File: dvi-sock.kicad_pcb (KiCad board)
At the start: 2 copper layers, 25.2 x 22.5 mm, 15 parts, among them J1 Conn_01x05, J2 Conn_01x05, J3 Conn_01x03, J4 NOT_HDMI_A, J5 2.54mm_2p_nofit

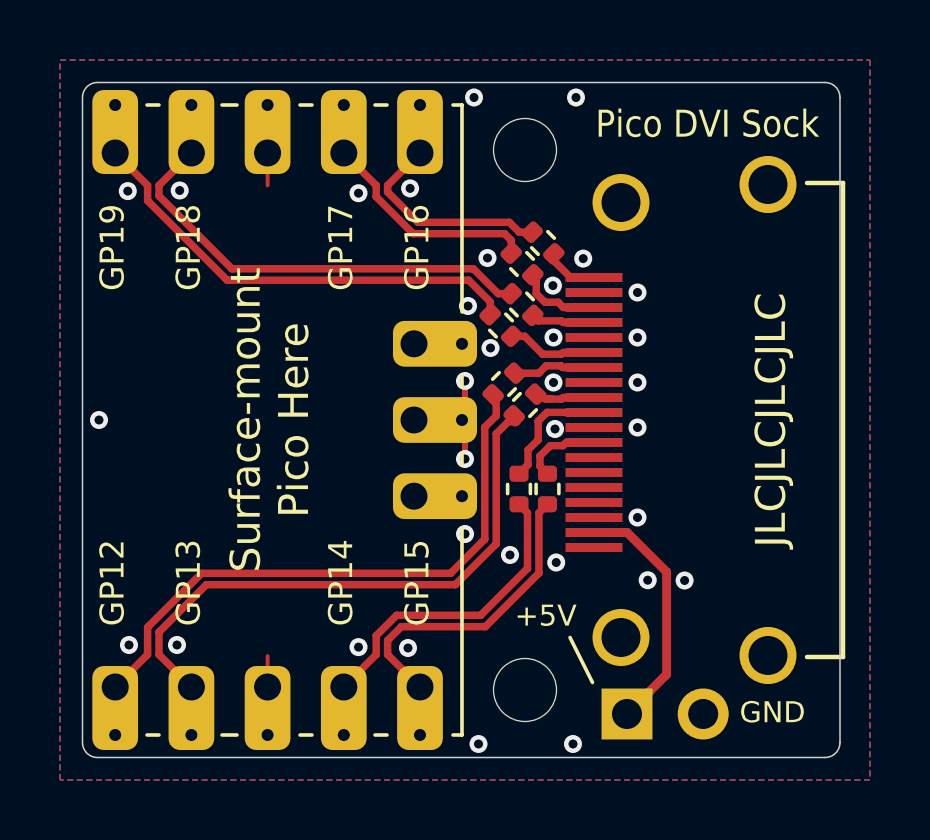
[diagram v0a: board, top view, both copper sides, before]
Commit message: Tweak silkscreen layout/orientation to match Pico
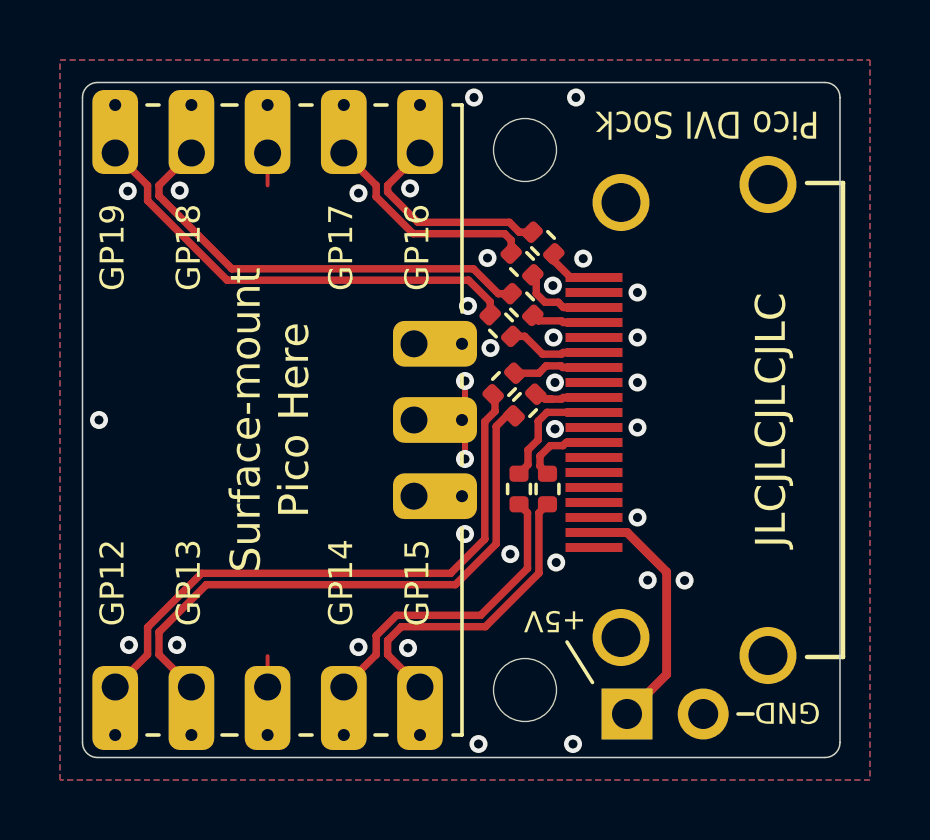
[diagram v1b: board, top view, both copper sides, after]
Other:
- board text added: "GP12: D0+ GP16: D2+ GP13: D0- GP17: D2- GP14: CK+ GP18: D1+ GP15: CK- GP19: D1-"
- board text removed: "GP12: D0+ GP13: D0- GP14: CK+ GP15: CK- GP16: D2+ GP17: D2- GP18: D1+ GP19: D1-"
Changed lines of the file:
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@@
     (pad "2" thru_hole oval (at 0 2.54 90) (locked) (size 1.7 1.7) (drill 1) (layers *.Cu *.Mask)
       (net 3 "GND") (pinfunction "Pin_2") (pintype "passive"))
-    (model "${KICAD6_3DMODEL_DIR}/Connector_PinHeader_2.54mm.3dshapes/PinHeader_1x02_P2.54mm_Vertical.wrl"
+    (model "${KICAD6_3DMODEL_DIR}/Connector_PinHeader_2.54mm.3dshapes/PinHeader_1x02_P2.54mm_Vertical.wrl" hide
       (offset (xyz 0 0 0))
       (scale (xyz 1 1 1))
@@
   (gr_line (start 154.4 81.4) (end 154.4 74.5) (layer "F.SilkS") (width 0.12))
   (gr_line (start 143.9 95.5) (end 144.3 95.5) (layer "F.SilkS") (width 0.12))
+  (gr_line (start 163.6 94.8) (end 164.1 94.8) (layer "F.SilkS") (width 0.12))
   (gr_line (start 144.3 74.5) (end 143.9 74.5) (layer "F.SilkS") (width 0.12))
   (gr_line (start 154.4 86.1) (end 154.4 86.5) (layer "F.SilkS") (width 0.12))
@@
   (gr_line (start 146.9 74.5) (end 146.4 74.5) (layer "F.SilkS") (width 0.12))
   (gr_line (start 149.4 74.5) (end 149 74.5) (layer "F.SilkS") (width 0.12))
-  (gr_line (start 158.75 93.75) (end 158 92.25) (layer "F.SilkS") (width 0.12))
+  (gr_line (start 158.75 93.75) (end 157.9 92.4) (layer "F.SilkS") (width 0.12))
   (gr_line (start 154.4 83.5) (end 154.4 83.9) (layer "F.SilkS") (width 0.12))
   (gr_line (start 154.4 95.5) (end 154.1 95.5) (layer "F.SilkS") (width 0.12))
@@
     (effects (font (size 1 1) (thickness 0.25)) (justify mirror))
   )
-  (gr_text "GP12: D0+\nGP13: D0-\nGP14: CK+\nGP15: CK-\nGP16: D2+\nGP17: D2-\nGP18: D1+\nGP19: D1-" (at 147 85) (layer "B.SilkS")
-    (effects (font (size 1 1) (thickness 0.15)) (justify mirror))
-  )
-  (gr_text "Rev A" (at 165.26 94.89) (layer "B.SilkS")
+  (gr_text "GP12: D0+ GP16: D2+\nGP13: D0- GP17: D2-\nGP14: CK+ GP18: D1+\nGP15: CK- GP19: D1-" (at 146.6 85 90) (layer "B.SilkS")
+    (effects (font (size 1 0.9) (thickness 0.13)) (justify mirror))
+  )
+  (gr_text "Rev A" (at 158.65 85.05 90) (layer "B.SilkS")
     (effects (font (size 0.7 0.7) (thickness 0.12)) (justify mirror))
   )
-  (gr_text "Pico DVI Sock" (at 162.58 75.14) (layer "F.SilkS")
+  (gr_text "Pico DVI Sock" (at 162.58 75.14 180) (layer "F.SilkS")
     (effects (font (size 0.9 0.8) (thickness 0.12)))
   )
@@
     (effects (font (size 0.8 0.8) (thickness 0.12)))
   )
-  (gr_text "+5V" (at 157.19 91.53) (layer "F.SilkS")
+  (gr_text "+5V" (at 157.5 91.7 180) (layer "F.SilkS")
     (effects (font (size 0.7 0.7) (thickness 0.12)))
   )
@@
     (effects (font (size 0.8 0.8) (thickness 0.12)))
   )
-  (gr_text "GND" (at 164.75 94.75) (layer "F.SilkS")
+  (gr_text "GND" (at 165.25 94.75 180) (layer "F.SilkS")
     (effects (font (size 0.7 0.7) (thickness 0.12)))
   )
@@
   (via (at 155.35 82.6) (size 0.6) (drill 0.3) (layers "F.Cu" "B.Cu") (free) (net 3))
   (via (at 143.26 77.37) (size 0.6) (drill 0.3) (layers "F.Cu" "B.Cu") (free) (net 3))
-  (via (at 156 89.5) (size 0.6) (drill 0.3) (layers "F.Cu" "B.Cu") (free) (net 3))
+  (via (at 156.01 89.47) (size 0.6) (drill 0.3) (layers "F.Cu" "B.Cu") (free) (net 3))
   (via (at 158.44 79.62) (size 0.6) (drill 0.3) (layers "F.Cu" "B.Cu") (free) (net 3))
   (via (at 154.5 86.3) (size 0.6) (drill 0.3) (layers "F.Cu" "B.Cu") (free) (net 3))
@@
   (via (at 154.8 74.25) (size 0.6) (drill 0.3) (layers "F.Cu" "B.Cu") (free) (net 3))
   (via (at 152.6 92.6) (size 0.6) (drill 0.3) (layers "F.Cu" "B.Cu") (free) (net 3))
-  (via (at 157.45 83.75) (size 0.6) (drill 0.3) (layers "F.Cu" "B.Cu") (free) (net 3))
+  (via (at 157.5 83.75) (size 0.6) (drill 0.3) (layers "F.Cu" "B.Cu") (free) (net 3))
   (via (at 154.6 81.2) (size 0.6) (drill 0.3) (layers "F.Cu" "B.Cu") (free) (net 3))
   (via (at 143.3 92.5) (size 0.6) (drill 0.3) (layers "F.Cu" "B.Cu") (free) (net 3))
@@
   (via (at 144.99 77.35) (size 0.6) (drill 0.3) (layers "F.Cu" "B.Cu") (free) (net 3))
   (via (at 150.95 77.44) (size 0.6) (drill 0.3) (layers "F.Cu" "B.Cu") (free) (net 3))
-  (segment (start 155.54 89.128702) (end 155.54 85.46) (width 0.25) (layer "F.Cu") (net 4))
+  (segment (start 155.54 89.128702) (end 155.54 85.21) (width 0.25) (layer "F.Cu") (net 4))
+  (segment (start 154.178702 90.49) (end 155.54 89.128702) (width 0.25) (layer "F.Cu") (net 4))
+  (segment (start 155.889376 84.860624) (end 156.139376 84.860624) (width 0.25) (layer "F.Cu") (net 4))
+  (segment (start 144.3 92.068702) (end 145.878702 90.49) (width 0.25) (layer "F.Cu") (net 4))
+  (segment (start 145.878702 90.49) (end 154.178702 90.49) (width 0.25) (layer "F.Cu") (net 4))
+  (segment (start 145.38 93.9) (end 144.3 92.82) (width 0.25) (layer "F.Cu") (net 4))
   (segment (start 144.3 92.82) (end 144.3 92.068702) (width 0.25) (layer "F.Cu") (net 4))
-  (segment (start 145.38 93.9) (end 144.3 92.82) (width 0.25) (layer "F.Cu") (net 4))
-  (segment (start 155.939376 85.060624) (end 156.239376 85.060624) (width 0.25) (layer "F.Cu") (net 4))
-  (segment (start 154.178702 90.49) (end 155.54 89.128702) (width 0.25) (layer "F.Cu") (net 4))
-  (segment (start 145.878702 90.49) (end 154.178702 90.49) (width 0.25) (layer "F.Cu") (net 4))
-  (segment (start 155.54 85.46) (end 155.939376 85.060624) (width 0.25) (layer "F.Cu") (net 4))
-  (segment (start 144.3 92.068702) (end 145.878702 90.49) (width 0.25) (layer "F.Cu") (net 4))
-  (segment (start 155.539376 84.860624) (end 155.539376 84.360624) (width 0.25) (layer "F.Cu") (net 5))
+  (segment (start 155.54 85.21) (end 155.889376 84.860624) (width 0.25) (layer "F.Cu") (net 4))
+  (segment (start 143.92 92.82) (end 143.92 91.911298) (width 0.25) (layer "F.Cu") (net 5))
+  (segment (start 155.5 84.71257) (end 155.5 84.221248) (width 0.25) (layer "F.Cu") (net 5))
+  (segment (start 155.5 84.221248) (end 155.439376 84.160624) (width 0.25) (layer "F.Cu") (net 5))
+  (segment (start 155.15998 88.971318) (end 155.15998 85.05259) (width 0.25) (layer "F.Cu") (net 5))
+  (segment (start 143.92 91.911298) (end 145.721298 90.11) (width 0.25) (layer "F.Cu") (net 5))
   (segment (start 145.721298 90.11) (end 154.021298 90.11) (width 0.25) (layer "F.Cu") (net 5))
-  (segment (start 154.021298 90.11) (end 155.15999 88.971308) (width 0.25) (layer "F.Cu") (net 5))
-  (segment (start 143.92 92.82) (end 143.92 91.911298) (width 0.25) (layer "F.Cu") (net 5))
   (segment (start 142.84 93.9) (end 143.92 92.82) (width 0.25) (layer "F.Cu") (net 5))
-  (segment (start 155.15999 85.24001) (end 155.539376 84.860624) (width 0.25) (layer "F.Cu") (net 5))
-  (segment (start 143.92 91.911298) (end 145.721298 90.11) (width 0.25) (layer "F.Cu") (net 5))
-  (segment (start 155.15999 88.971308) (end 155.15999 85.24001) (width 0.25) (layer "F.Cu") (net 5))
+  (segment (start 155.15998 85.05259) (end 155.5 84.71257) (width 0.25) (layer "F.Cu") (net 5))
+  (segment (start 154.021298 90.11) (end 155.15998 88.971318) (width 0.25) (layer "F.Cu") (net 5))
   (segment (start 142.84 76.1) (end 143.92 77.18) (width 0.25) (layer "F.Cu") (net 6))
   (segment (start 143.92 77.688702) (end 146.571298 80.34) (width 0.25) (layer "F.Cu") (net 6))
